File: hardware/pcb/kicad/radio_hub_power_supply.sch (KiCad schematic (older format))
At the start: 21 parts

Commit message: Schematic "done" - resolving ERC
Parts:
- removed C?: C, ~, symbol C
- added C10A: C, ~, symbol C
- added R10A, R11A, R14, R9A, RNEW: R, ~, symbol R
- gave numbers to parts that had none: 20
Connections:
- net +3V3: now also C9.1; no longer C7A.1, R7A.1
- net 2V8_A: now also C10A.1; no longer C12A.1, IC8A.5 (VO)
- net GND: now also R14.2, R9A.1, RNEW.2; no longer C10.2, C11.2, C11A.2, C12.2, C12A.2, C13.2, C9.2, D1.1 (A), IC4.2 (GND), IC8A.2 (GND), L3.3, R14.2
- net GNDA: now reaches C8A.2, C9A.2, D1A.1 (A), IC7A.2 (GND), R8A.2
- net GNDA: now also C11A.2, C12A.2, IC8A.2 (GND), C10A.2, R10A.1, R10A.2, R11A.1, R11A.2, R9A.2
- net GNDINT: now reaches C7A.2, R8A.1
- net GNDINT: now also C10.2, C11.2, C12.2, C13.2, C9.2, D1.1 (A), IC4.2 (GND), L3.3, R14.2, R14.1, RNEW.1
- net at IC3.3 (VO): now also C7A.1, R7A.1; no longer C9.1
- new net 2V8_B: C12A.1, IC8A.5 (VO)
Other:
- moved on the sheet: C10, C11, C11A, C12, C12A, C13, C7A, C8A, C9, C9A, D1, D1A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

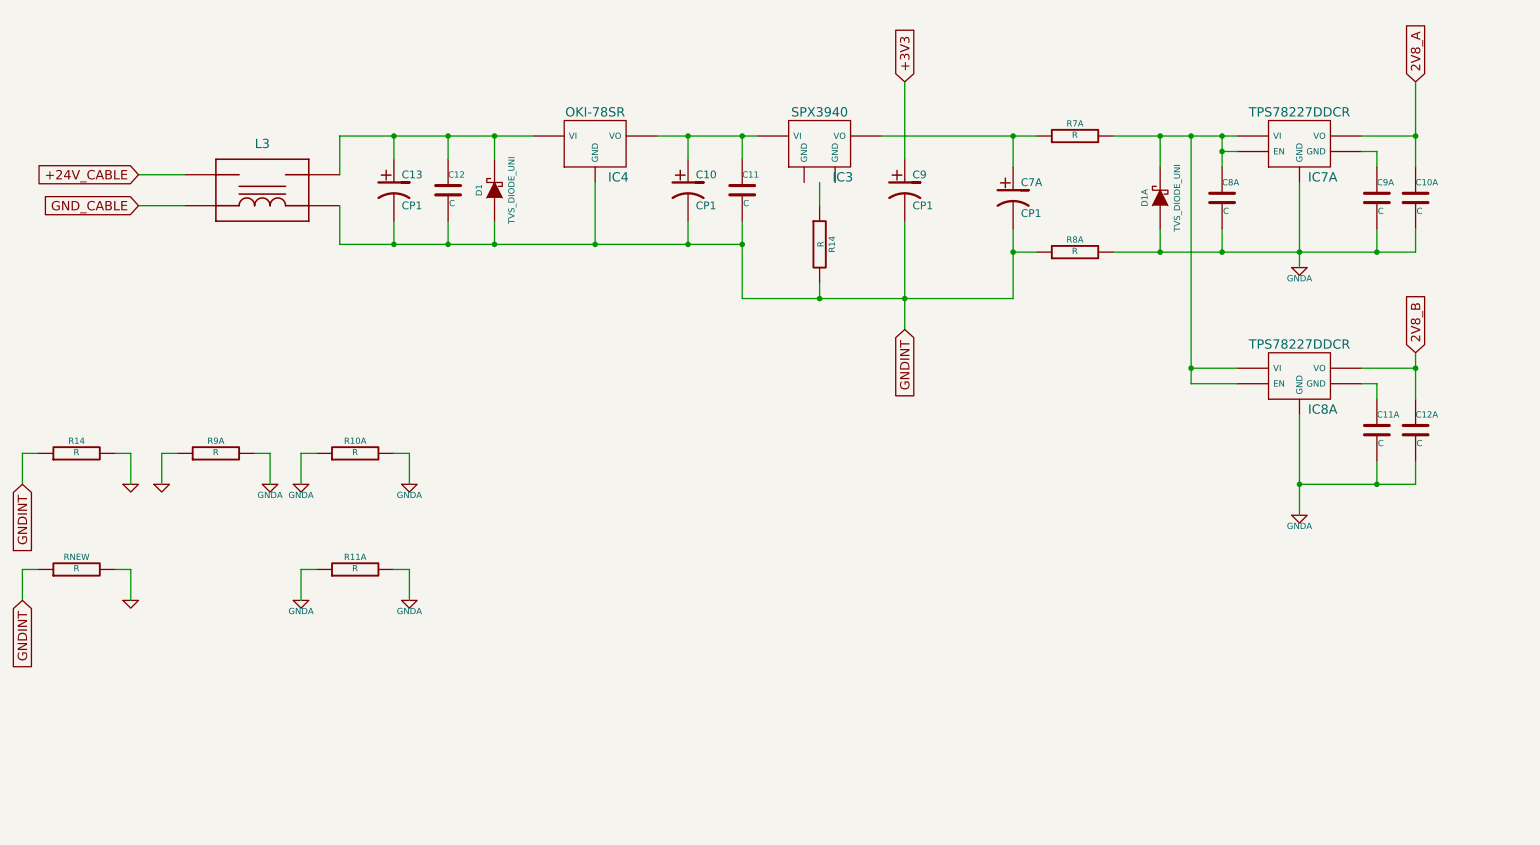
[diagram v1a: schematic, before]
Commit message: Component values added to schematic. Schematic now passes ERC
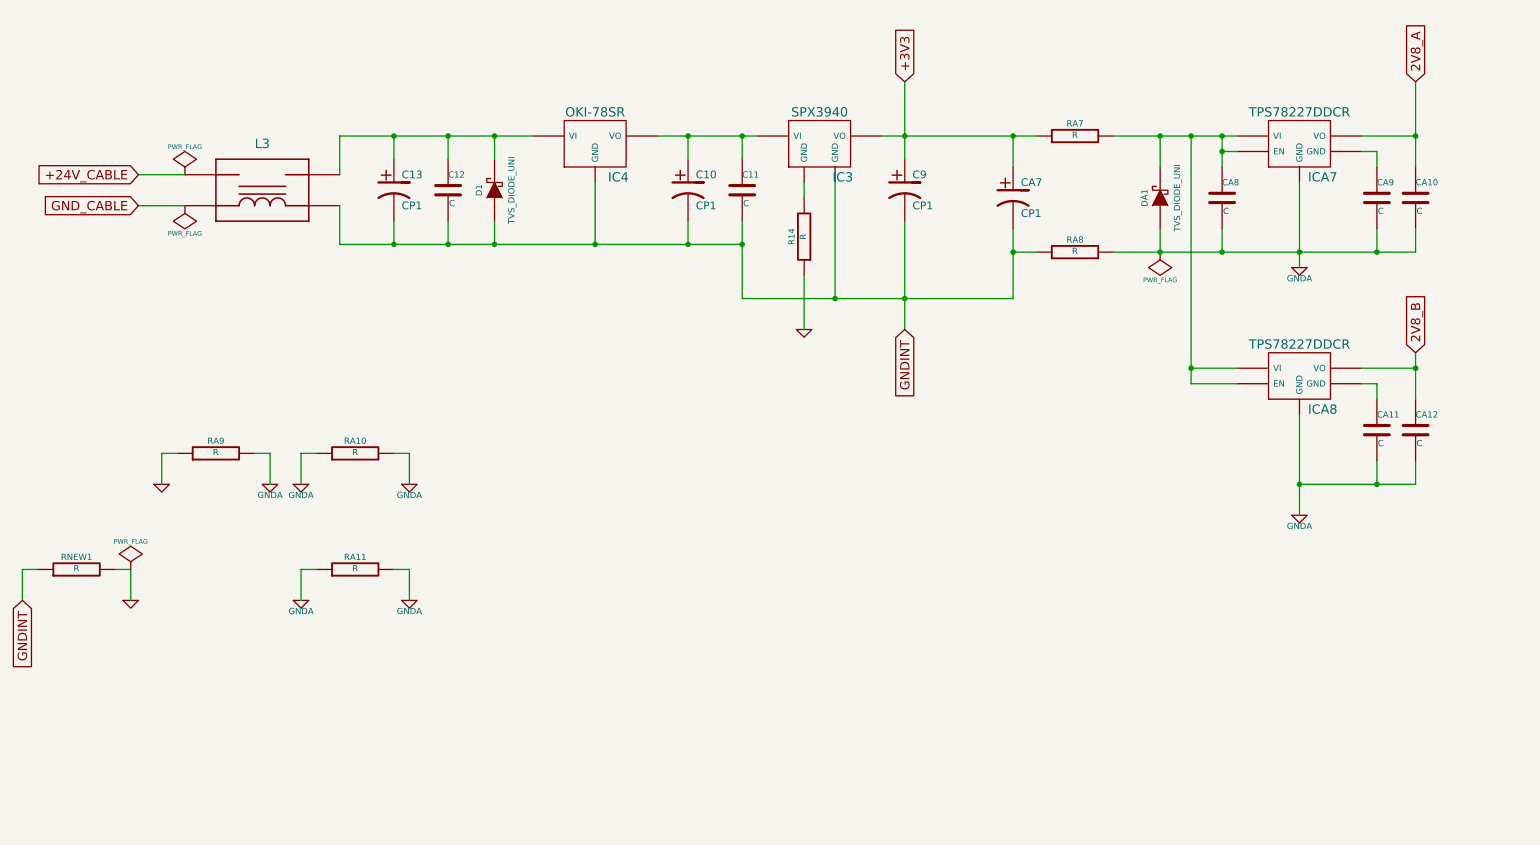
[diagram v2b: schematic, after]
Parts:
- removed R14: R, ~, symbol R
- renumbered C10A to CA10, C11A to CA11, C12A to CA12, C7A to CA7, C8A to CA8, C9A to CA9, D1A to DA1, IC7A to ICA7, IC8A to ICA8, R10A to RA10, R11A to RA11, R7A to RA7, R8A to RA8, R9A to RA9, RNEW to RNEW1
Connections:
- net +3V3: now also CA7.1, IC3.3 (VO), RA7.1
- net GND: now also R14.1; no longer R14.2
- net GNDINT: now also IC3.4 (GND); no longer R14.1
- net at IC3.2 (GND): now also R14.2
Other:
- moved on the sheet: R14

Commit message: Added a power switch
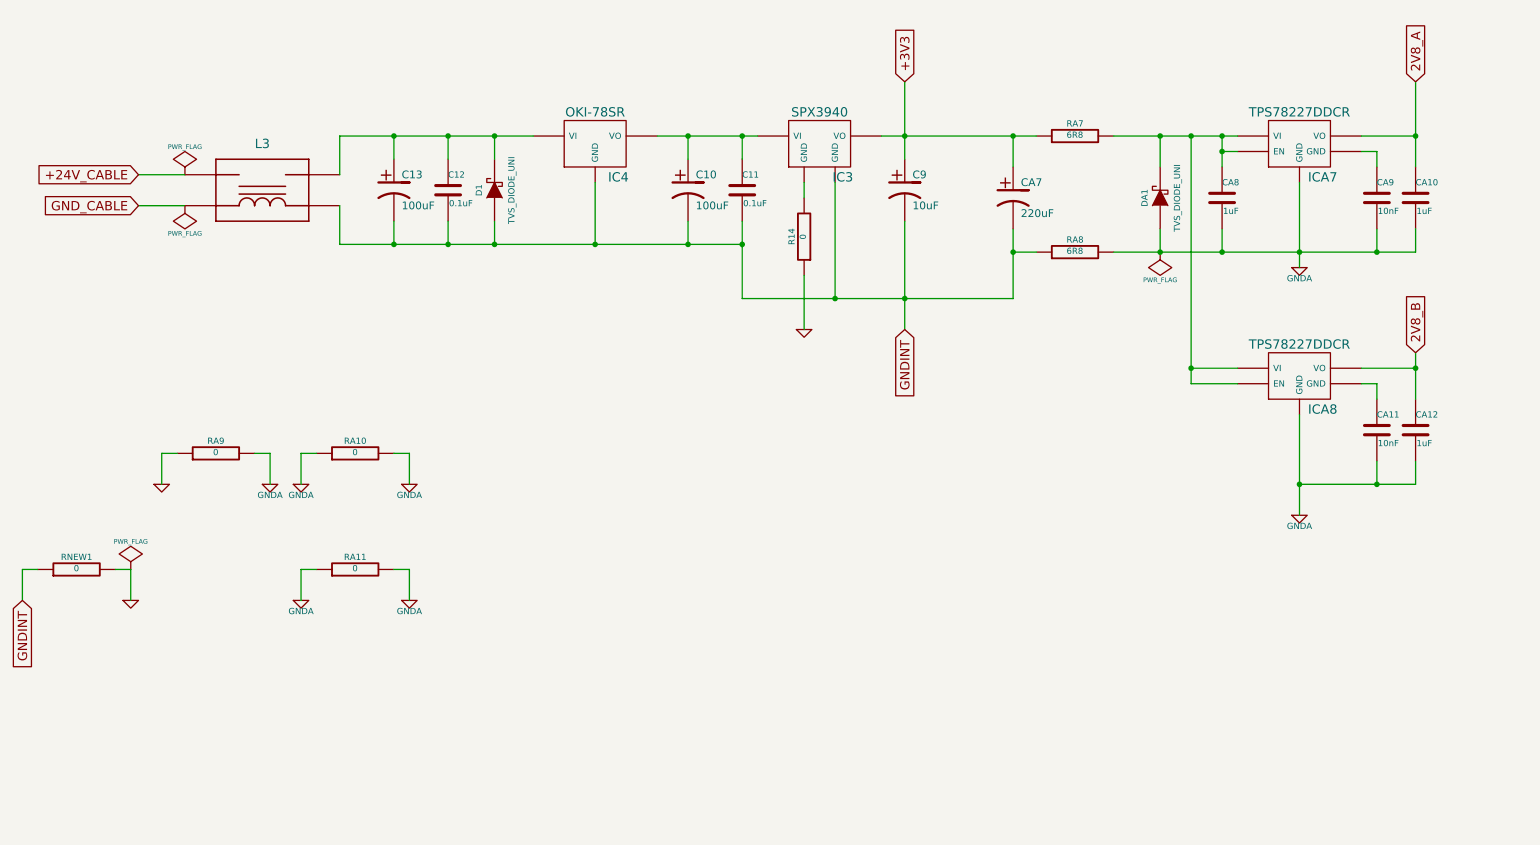
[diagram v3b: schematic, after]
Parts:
- C10, C13: value CP1 -> 100uF
- C11, C12: value C -> 0.1uF
- C9: value CP1 -> 10uF
- CA10, CA12, CA8: value C -> 1uF
- CA11, CA9: value C -> 10nF
- CA7: value CP1 -> 220uF
- R14, RA10, RA11, RA9, RNEW1: value R -> 0
- RA7, RA8: value R -> 6R8
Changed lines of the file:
@@
 P 10000 1750
 F 0 "CA9" H 10000 1850 40  0000 L CNN
-F 1 "C" H 10006 1665 40  0000 L CNN
+F 1 "10nF" H 10006 1665 40  0000 L CNN
 F 2 "~" H 10038 1600 30  0000 C CNN
 F 3 "~" H 10000 1750 60  0000 C CNN
@@
 P 9000 1750
 F 0 "CA8" H 9000 1850 40  0000 L CNN
-F 1 "C" H 9006 1665 40  0000 L CNN
+F 1 "1uF" H 9006 1665 40  0000 L CNN
 F 2 "~" H 9038 1600 30  0000 C CNN
 F 3 "~" H 9000 1750 60  0000 C CNN
@@
 P 8050 1350
 F 0 "RA7" V 8130 1350 40  0000 C CNN
-F 1 "R" V 8057 1351 40  0000 C CNN
+F 1 "6R8" V 8057 1351 40  0000 C CNN
 F 2 "~" V 7980 1350 30  0000 C CNN
 F 3 "~" H 8050 1350 30  0000 C CNN
@@
 P 8050 2100
 F 0 "RA8" V 8130 2100 40  0000 C CNN
-F 1 "R" V 8057 2101 40  0000 C CNN
+F 1 "6R8" V 8057 2101 40  0000 C CNN
 F 2 "~" V 7980 2100 30  0000 C CNN
 F 3 "~" H 8050 2100 30  0000 C CNN
@@
 P 7650 1750
 F 0 "CA7" H 7700 1850 50  0000 L CNN
-F 1 "CP1" H 7700 1650 50  0000 L CNN
+F 1 "220uF" H 7700 1650 50  0000 L CNN
 F 2 "~" H 7650 1750 60  0000 C CNN
 F 3 "~" H 7650 1750 60  0000 C CNN
@@
 P 10000 3250
 F 0 "CA11" H 10000 3350 40  0000 L CNN
-F 1 "C" H 10006 3165 40  0000 L CNN
+F 1 "10nF" H 10006 3165 40  0000 L CNN
 F 2 "~" H 10038 3100 30  0000 C CNN
 F 3 "~" H 10000 3250 60  0000 C CNN
@@
 P 10250 3250
 F 0 "CA12" H 10250 3350 40  0000 L CNN
-F 1 "C" H 10256 3165 40  0000 L CNN
+F 1 "1uF" H 10256 3165 40  0000 L CNN
 F 2 "~" H 10288 3100 30  0000 C CNN
 F 3 "~" H 10250 3250 60  0000 C CNN
@@
 P 4000 1700
 F 0 "C12" H 4000 1800 40  0000 L CNN
-F 1 "C" H 4006 1615 40  0000 L CNN
+F 1 "0.1uF" H 4006 1615 40  0000 L CNN
 F 2 "~" H 4038 1550 30  0000 C CNN
 F 3 "~" H 4000 1700 60  0000 C CNN
@@
 P 3650 1700
 F 0 "C13" H 3700 1800 50  0000 L CNN
-F 1 "CP1" H 3700 1600 50  0000 L CNN
+F 1 "100uF" H 3700 1600 50  0000 L CNN
 F 2 "~" H 3650 1700 60  0000 C CNN
 F 3 "~" H 3650 1700 60  0000 C CNN
@@
 P 5550 1700
 F 0 "C10" H 5600 1800 50  0000 L CNN
-F 1 "CP1" H 5600 1600 50  0000 L CNN
+F 1 "100uF" H 5600 1600 50  0000 L CNN
 F 2 "~" H 5550 1700 60  0000 C CNN
 F 3 "~" H 5550 1700 60  0000 C CNN
@@
 P 5900 1700
 F 0 "C11" H 5900 1800 40  0000 L CNN
-F 1 "C" H 5906 1615 40  0000 L CNN
+F 1 "0.1uF" H 5906 1615 40  0000 L CNN
 F 2 "~" H 5938 1550 30  0000 C CNN
 F 3 "~" H 5900 1700 60  0000 C CNN
@@
 P 6950 1700
 F 0 "C9" H 7000 1800 50  0000 L CNN
-F 1 "CP1" H 7000 1600 50  0000 L CNN
+F 1 "10uF" H 7000 1600 50  0000 L CNN
 F 2 "~" H 6950 1700 60  0000 C CNN
 F 3 "~" H 6950 1700 60  0000 C CNN
@@
 P 2500 3400
 F 0 "RA9" V 2580 3400 40  0000 C CNN
-F 1 "R" V 2507 3401 40  0000 C CNN
+F 1 "0" V 2507 3401 40  0000 C CNN
 F 2 "~" V 2430 3400 30  0000 C CNN
 F 3 "~" H 2500 3400 30  0000 C CNN
@@
 P 3400 3400
 F 0 "RA10" V 3480 3400 40  0000 C CNN
-F 1 "R" V 3407 3401 40  0000 C CNN
+F 1 "0" V 3407 3401 40  0000 C CNN
 F 2 "~" V 3330 3400 30  0000 C CNN
 F 3 "~" H 3400 3400 30  0000 C CNN
@@
 P 3400 4150
 F 0 "RA11" V 3480 4150 40  0000 C CNN
-F 1 "R" V 3407 4151 40  0000 C CNN
+F 1 "0" V 3407 4151 40  0000 C CNN
 F 2 "~" V 3330 4150 30  0000 C CNN
 F 3 "~" H 3400 4150 30  0000 C CNN
@@
 P 6300 2000
 F 0 "R14" V 6380 2000 40  0000 C CNN
-F 1 "R" V 6307 2001 40  0000 C CNN
+F 1 "0" V 6307 2001 40  0000 C CNN
 F 2 "~" V 6230 2000 30  0000 C CNN
 F 3 "~" H 6300 2000 30  0000 C CNN
@@
 P 1600 4150
 F 0 "RNEW1" V 1680 4150 40  0000 C CNN
-F 1 "R" V 1607 4151 40  0000 C CNN
+F 1 "0" V 1607 4151 40  0000 C CNN
 F 2 "~" V 1530 4150 30  0000 C CNN
 F 3 "~" H 1600 4150 30  0000 C CNN
@@
 P 10250 1750
 F 0 "CA10" H 10250 1850 40  0000 L CNN
-F 1 "C" H 10256 1665 40  0000 L CNN
+F 1 "1uF" H 10256 1665 40  0000 L CNN
 F 2 "~" H 10288 1600 30  0000 C CNN
 F 3 "~" H 10250 1750 60  0000 C CNN

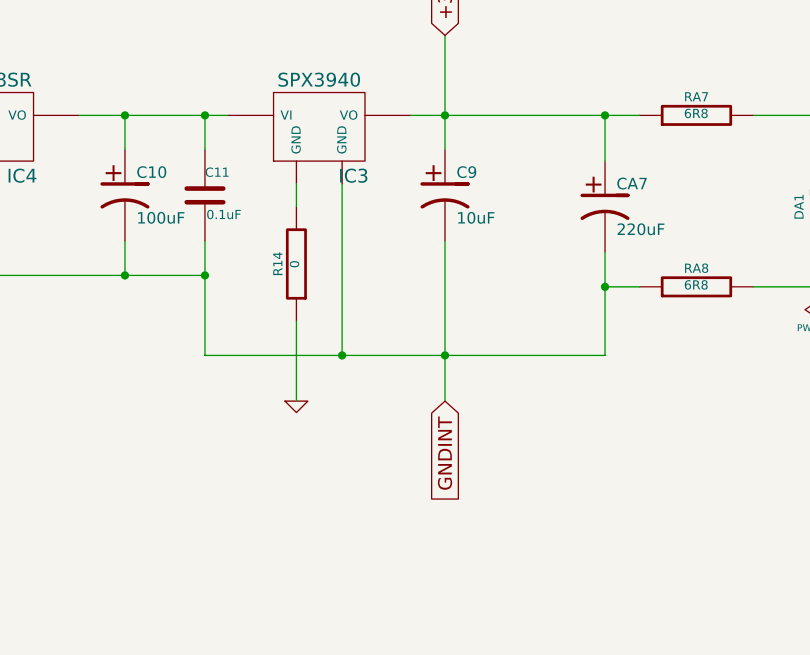
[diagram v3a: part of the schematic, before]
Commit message: Address connectivity issues. Removal of connectors and rerouting of tracks
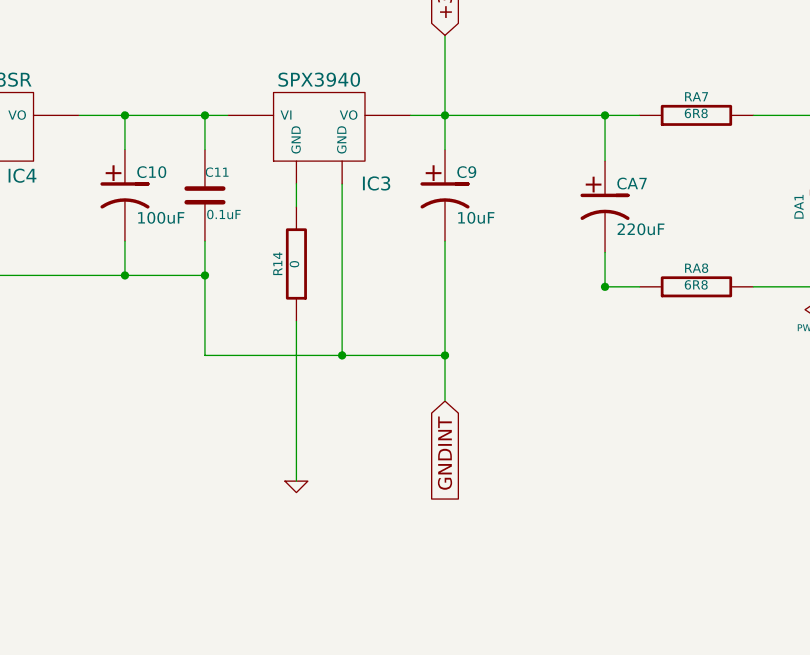
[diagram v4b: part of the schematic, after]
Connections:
- net GNDINT: no longer CA7.2, RA8.1
- new net: CA7.2, RA8.1
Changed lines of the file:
@@
 Sheet 2 3
 Title "noname.sch"
-Date "11 nov 2014"
+Date "21 nov 2014"
 Rev ""
 Comp ""
@@
 	6800 1350 7800 1350
 Wire Wire Line
-	7650 2400 7650 1950
-Wire Wire Line
 	7650 2100 7800 2100
 Wire Wire Line
@@
 U 1 1 545AE4FA
 P 6400 1400
-F 0 "IC3" H 6550 1184 60  0000 C CNN
+F 0 "IC3" H 6650 1150 60  0000 C CNN
 F 1 "SPX3940_TART" H 6400 1710 60  0001 C CNN
 F 2 "~" H 6400 1400 60  0000 C CNN
@@
 	1    0    0    -1
 $EndComp
-Wire Wire Line
-	5900 2400 7650 2400
 Connection ~ 6950 2400
 Text GLabel 6950 2600 3    60   Input ~ 0
@@
 L GND #PWR034
 U 1 1 545FE68B
-P 6300 2600
-F 0 "#PWR034" H 6300 2600 30  0001 C CNN
-F 1 "GND" H 6300 2530 30  0001 C CNN
-F 2 "" H 6300 2600 60  0000 C CNN
-F 3 "" H 6300 2600 60  0000 C CNN
-	1    6300 2600
+P 6300 2950
+F 0 "#PWR034" H 6300 2950 30  0001 C CNN
+F 1 "GND" H 6300 2880 30  0001 C CNN
+F 2 "" H 6300 2950 60  0000 C CNN
+F 3 "" H 6300 2950 60  0000 C CNN
+	1    6300 2950
 	1    0    0    -1
 $EndComp
@@
 	6300 1650 6300 1750
 Wire Wire Line
-	6300 2250 6300 2600
+	6300 2250 6300 2950
 $Comp
 L PWR_FLAG #FLG038
@@
 	1    0    0    -1
 $EndComp
+Wire Wire Line
+	7650 1950 7650 2100
+Wire Wire Line
+	5900 2400 6950 2400
 $EndSCHEMATC

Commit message: Backup
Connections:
- net GND: no longer R14.1
- net GNDINT: no longer C9.2
- net at IC3.2 (GND), R14.2: now also C9.2
- new net DGND: R14.1
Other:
- moved on the sheet: R14

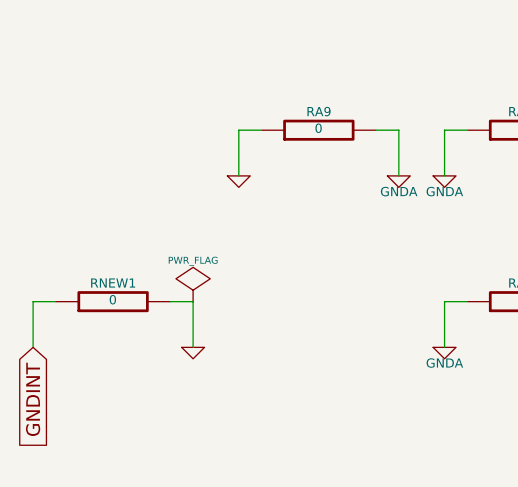
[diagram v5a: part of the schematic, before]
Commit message: Base station and radio hub boards ready for final checks before manufacture
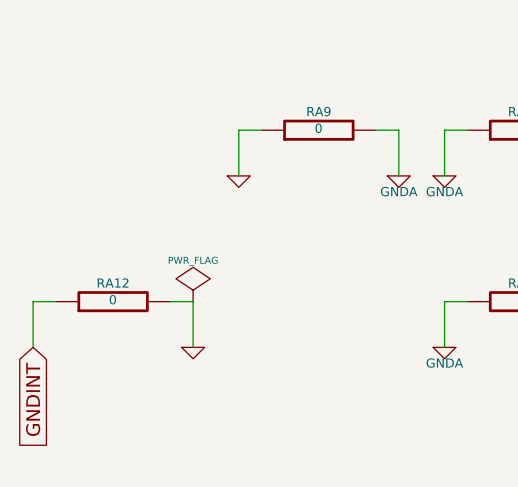
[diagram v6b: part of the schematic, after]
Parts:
- renumbered RNEW1 to RA12
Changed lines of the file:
@@
 Sheet 2 3
 Title "noname.sch"
-Date "26 nov 2014"
+Date "3 dec 2014"
 Rev ""
 Comp ""
@@
 $EndComp
 $Comp
-L R RNEW1
+L R RA12
 U 1 1 545FE6B7
 P 1600 4150
-F 0 "RNEW1" V 1680 4150 40  0000 C CNN
+F 0 "RA12" V 1680 4150 40  0000 C CNN
 F 1 "0" V 1607 4151 40  0000 C CNN
 F 2 "~" V 1530 4150 30  0000 C CNN
